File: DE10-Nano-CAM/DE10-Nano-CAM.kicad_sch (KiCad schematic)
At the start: 29 parts, among them J1 DF40C-100DS-0.4V_51_, J2 DF40C-100DS-0.4V_51_, J3 MEM2075-00-140-01-A, J4 HDMI_A, J5 52271-1579

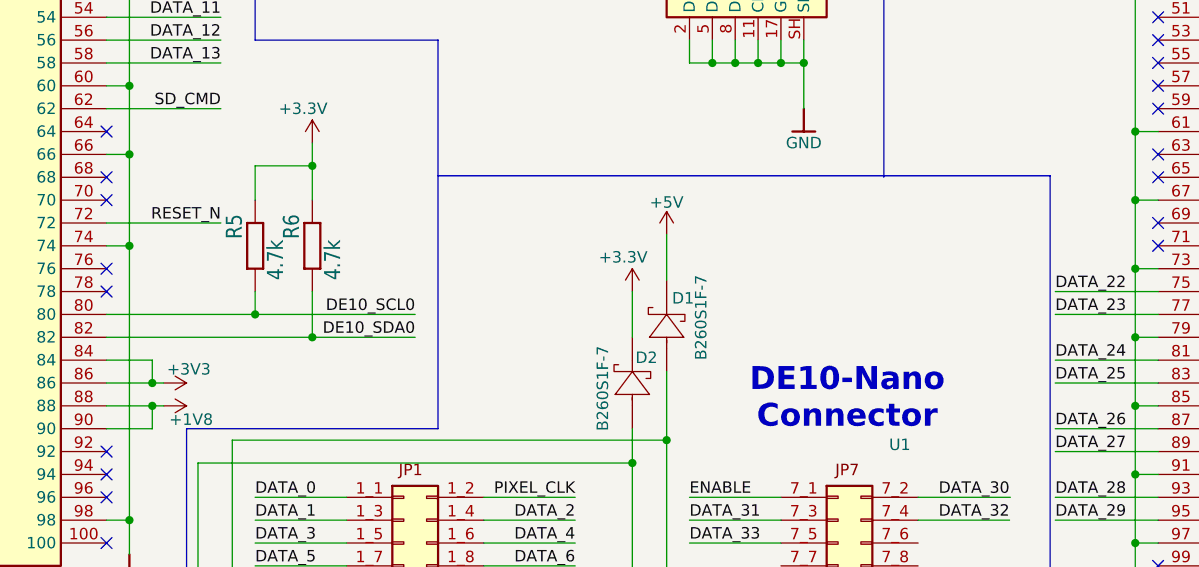
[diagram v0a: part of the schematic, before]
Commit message: changed initial pcb layout
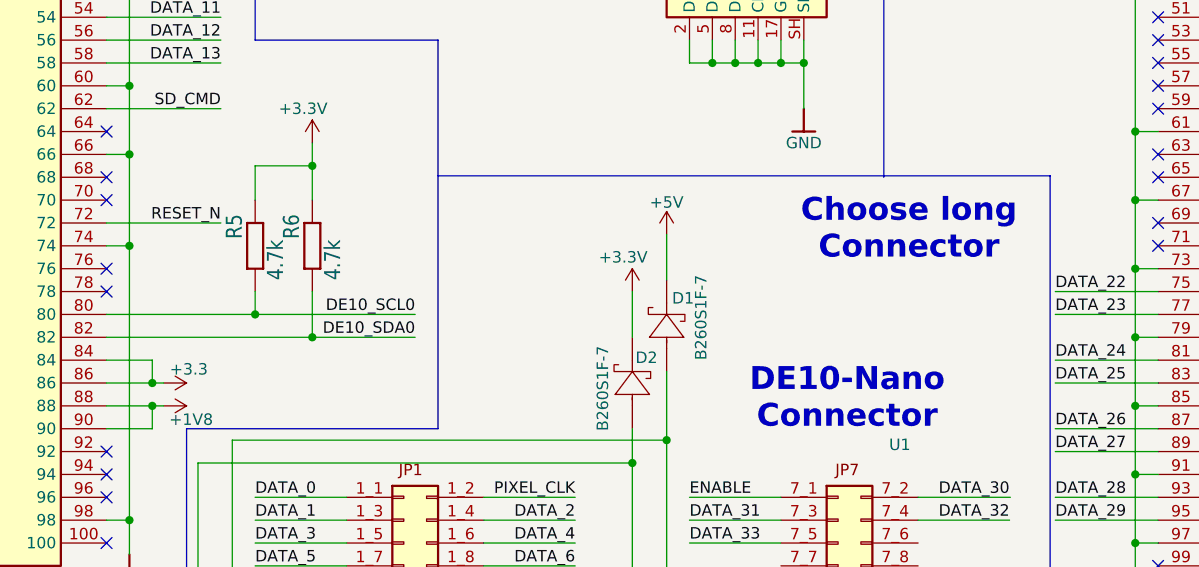
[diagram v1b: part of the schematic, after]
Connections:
- net +3V3 renamed +3.3
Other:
- note added: "Choose long Connector"

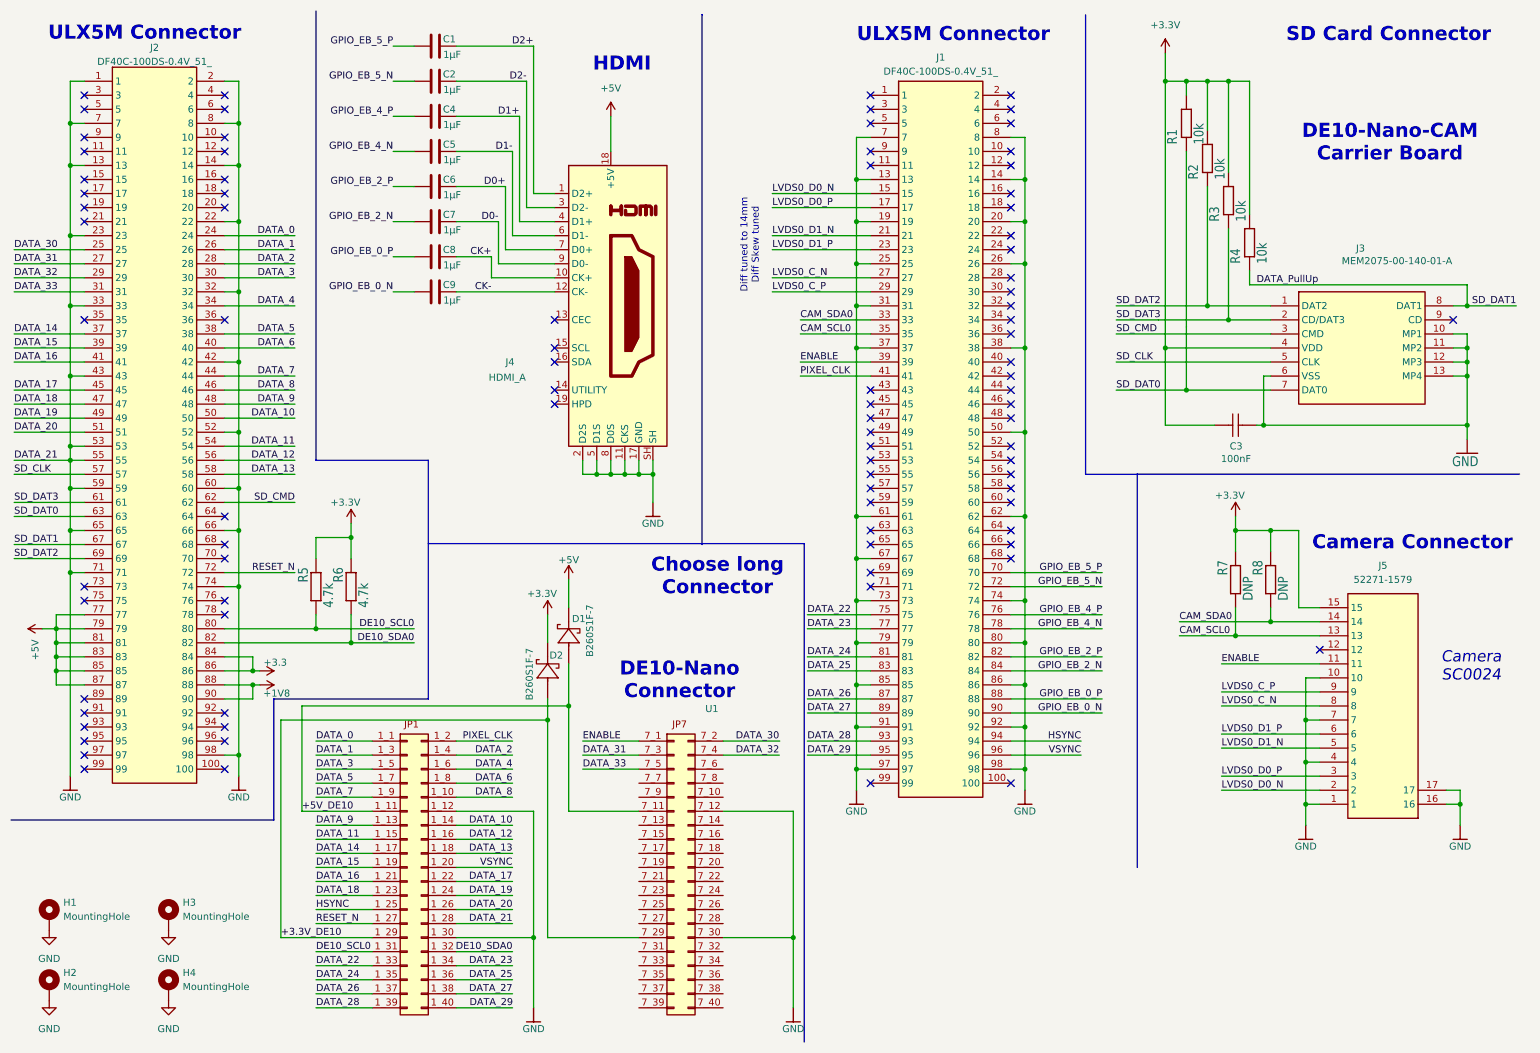
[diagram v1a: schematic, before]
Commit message: final v1 PCB design. Missing via stitching
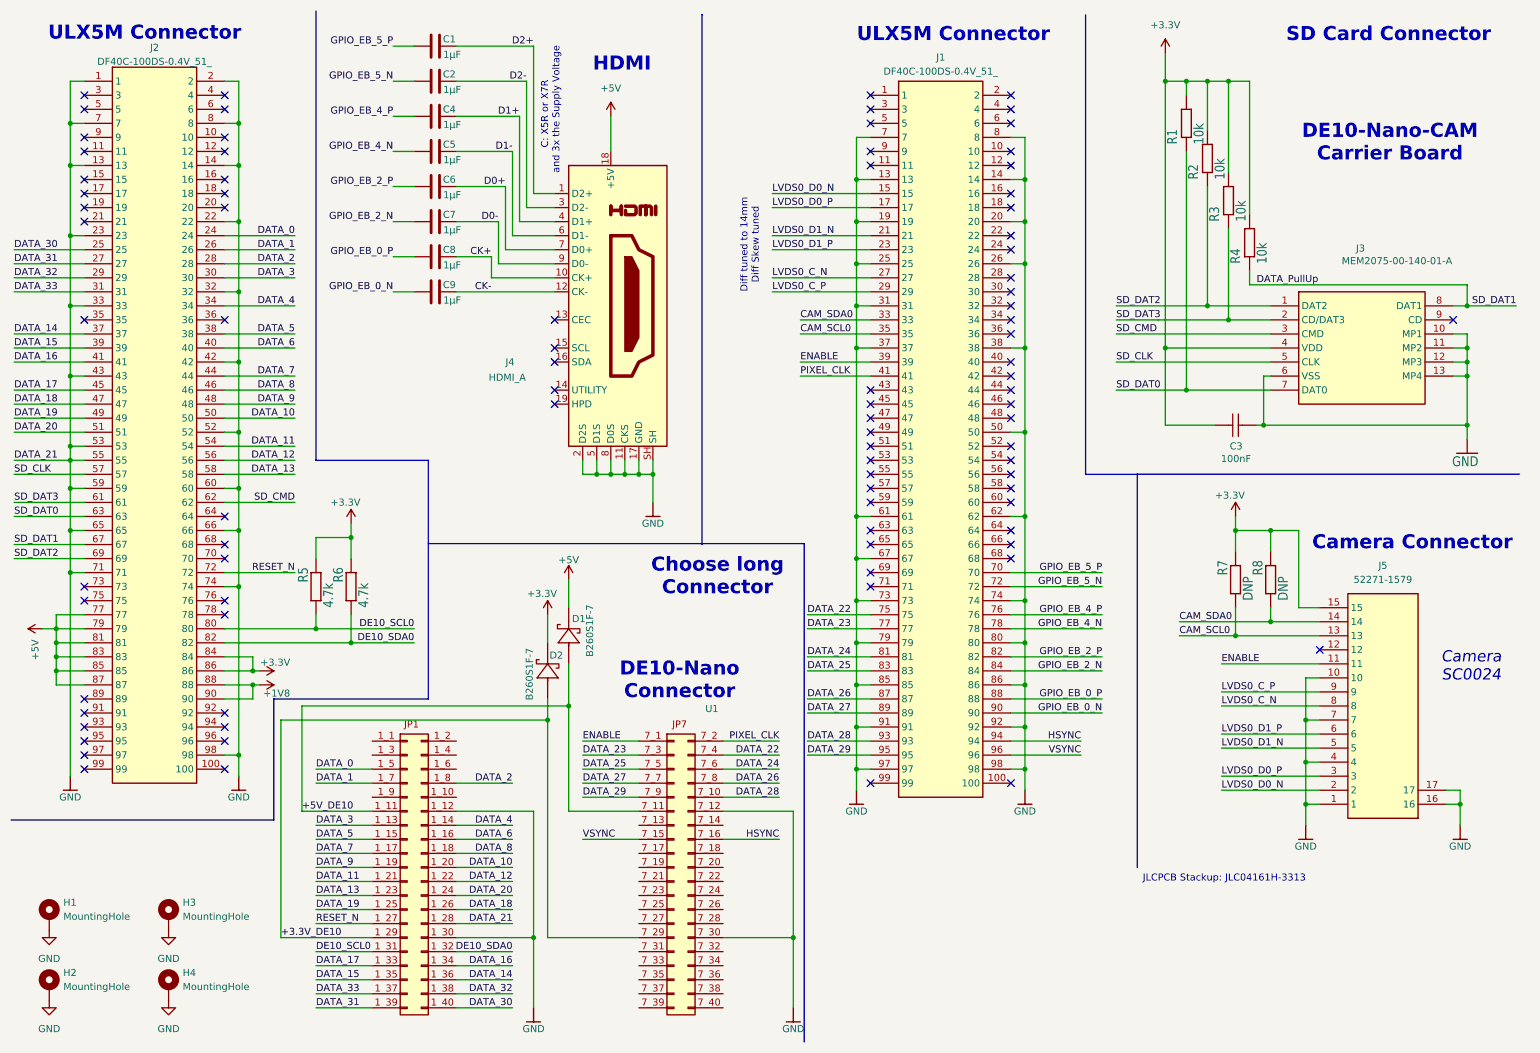
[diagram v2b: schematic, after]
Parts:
- C1, C2, C4, C5, C6, C7, C8, C9: footprint Capacitor_SMD:C_0603_1608Metric_Pad1.08x0.95mm_HandSolder -> Capacitor_SMD:C_0402_1005Metric
- R1, R2, R3, R4: footprint Resistor_SMD:R_0603_1608Metric -> Resistor_SMD:R_0402_1005Metric
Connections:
- net +3.3 is gone; now on net +3.3V: J2.84, J2.86
- net DATA_0: now also U1.1_5; no longer U1.1_1
- net DATA_1: now also U1.1_7; no longer U1.1_3
- net DATA_10: now also U1.1_20; no longer U1.1_14
- net DATA_11: now also U1.1_21; no longer U1.1_15
- net DATA_12: now also U1.1_22; no longer U1.1_16
- net DATA_13: now also U1.1_23; no longer U1.1_18
- net DATA_14: now also U1.1_36; no longer U1.1_17
- net DATA_15: now also U1.1_35; no longer U1.1_19
- net DATA_16: now also U1.1_34; no longer U1.1_21
- net DATA_17: now also U1.1_33; no longer U1.1_22
- net DATA_18: now also U1.1_26; no longer U1.1_23
- net DATA_19: now also U1.1_25; no longer U1.1_24
- net DATA_2: now also U1.1_8; no longer U1.1_4
- net DATA_20: now also U1.1_24; no longer U1.1_26
- net DATA_22: now also U1.7_4; no longer U1.1_33
- net DATA_23: now also U1.7_3; no longer U1.1_34
- net DATA_24: now also U1.7_6; no longer U1.1_35
- net DATA_25: now also U1.7_5; no longer U1.1_36
- net DATA_26: now also U1.7_8; no longer U1.1_37
- net DATA_27: now also U1.7_7; no longer U1.1_38
- net DATA_28: now also U1.7_10; no longer U1.1_39
- net DATA_29: now also U1.7_9
- net DATA_3: now also U1.1_13; no longer U1.1_5
- net DATA_30: now also U1.1_40; no longer U1.7_2
- net DATA_31: now also U1.1_39; no longer U1.7_3
- net DATA_32: now also U1.1_38; no longer U1.7_4
- net DATA_33: now also U1.1_37; no longer U1.7_5
- net DATA_4: now also U1.1_14; no longer U1.1_6
- net DATA_5: now also U1.1_15; no longer U1.1_7
- net DATA_6: now also U1.1_16; no longer U1.1_8
- net DATA_7: now also U1.1_17; no longer U1.1_9
- net DATA_8: now also U1.1_18; no longer U1.1_10
- net DATA_9: now also U1.1_19; no longer U1.1_13
- net GND: now also U1.7_12, U1.7_30
- net HSYNC: now also U1.7_16; no longer U1.1_25
- net PIXEL_CLK: now also U1.7_2; no longer U1.1_2
- net VSYNC: now also U1.7_15; no longer U1.1_20
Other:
- note added: "C: X5R or X7R and 3x the Supply Voltage"
- note added: "JLCPCB Stackup: JLC04161H-3313"
